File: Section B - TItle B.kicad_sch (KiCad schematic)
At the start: 2 parts

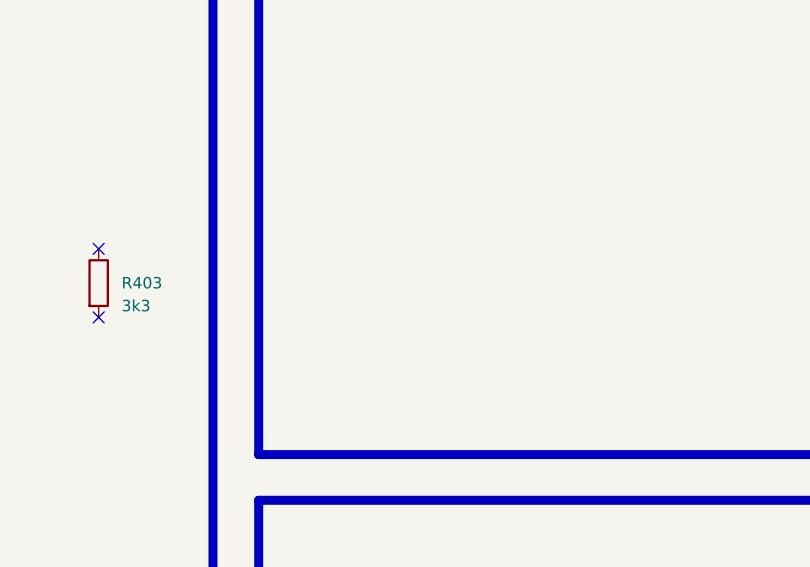
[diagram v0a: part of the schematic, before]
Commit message: section-b: CAN termination R405
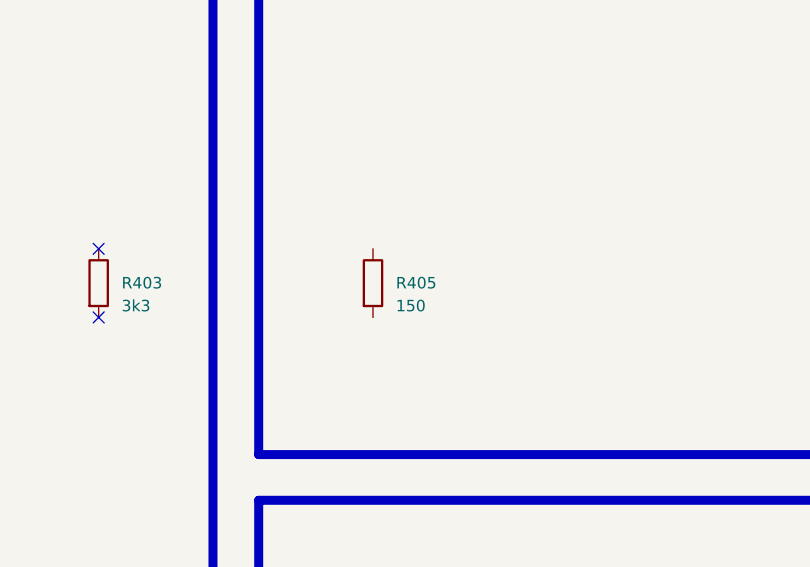
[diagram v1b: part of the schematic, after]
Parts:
- added R405: 150, Resistor_SMD:R_0603_1608Metric, symbol Device:R
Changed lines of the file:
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@@
+		)
+	)
+	(symbol
+		(lib_id "Device:R")
+		(at 152.4 101.6 0)
+		(unit 1)
+		(exclude_from_sim no)
+		(in_bom yes)
+		(on_board yes)
+		(dnp no)
+		(property "Reference" "R405"
+			(at 154.94 101.6 0)
+			(effects (font (size 1.27 1.27)) (justify left))
+		)
+		(property "Value" "150"
+			(at 154.94 104.14 0)
+			(effects (font (size 1.27 1.27)) (justify left))
+		)
+		(property "Footprint" "Resistor_SMD:R_0603_1608Metric"
+			(at 152.4 101.6 0)
+			(effects (font (size 1.27 1.27)) (hide yes))
+		)
+		(property "Datasheet" "~"
+			(at 152.4 101.6 0)
+			(effects (font (size 1.27 1.27)) (hide yes))
+		)
+		(pin "1")
+		(pin "2")
+		(instances
+			(project "ci_dummy"
+				(path "/f9e05184-c88b-4a88-ae9c-ab2bdb32be7c/c5103ceb-5325-4a84-a025-9638a412984e/e744f3ce-03a6-44a6-8792-1447ef232b9a"
+					(reference "R405")
+					(unit 1)
+				)
+			)
 		)
 	)

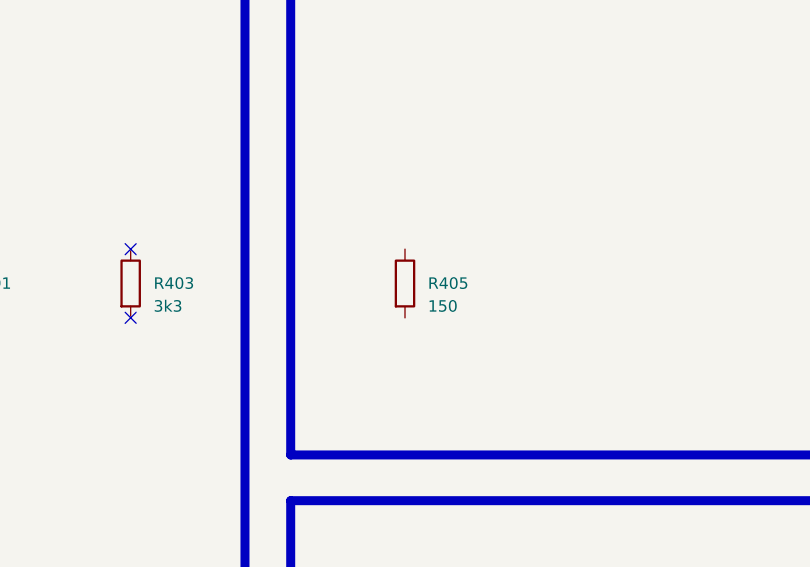
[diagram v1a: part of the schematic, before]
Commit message: dev: no-connects + footprints for R304/R405 before release
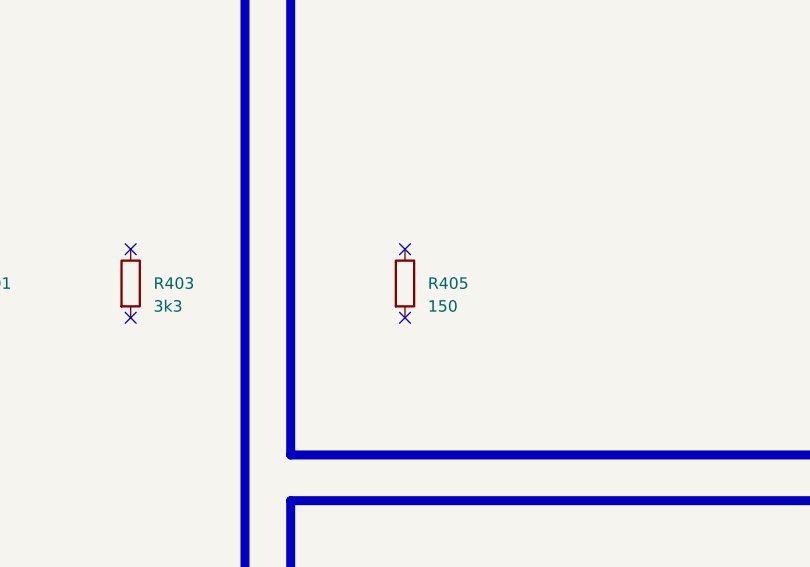
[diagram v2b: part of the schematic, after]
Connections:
- no-connect marks 4 -> 6
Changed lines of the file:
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@@
 		(at 121.92 105.41)
+	)
+	(no_connect
+		(at 152.4 97.79)
+	)
+	(no_connect
+		(at 152.4 105.41)
 	)
 	(symbol
